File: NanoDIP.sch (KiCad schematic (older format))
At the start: 13 parts, among them SW1 SW_Push, U1 LM7805_TO220, U2 ATMEGA328P-PU, Y1 16 MHz

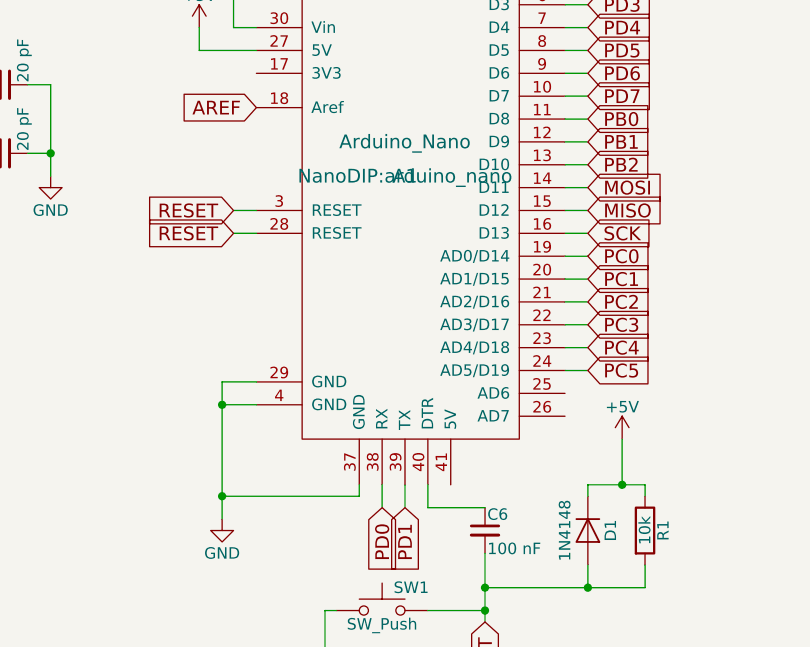
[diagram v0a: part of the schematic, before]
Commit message: Added 5V pin to program header
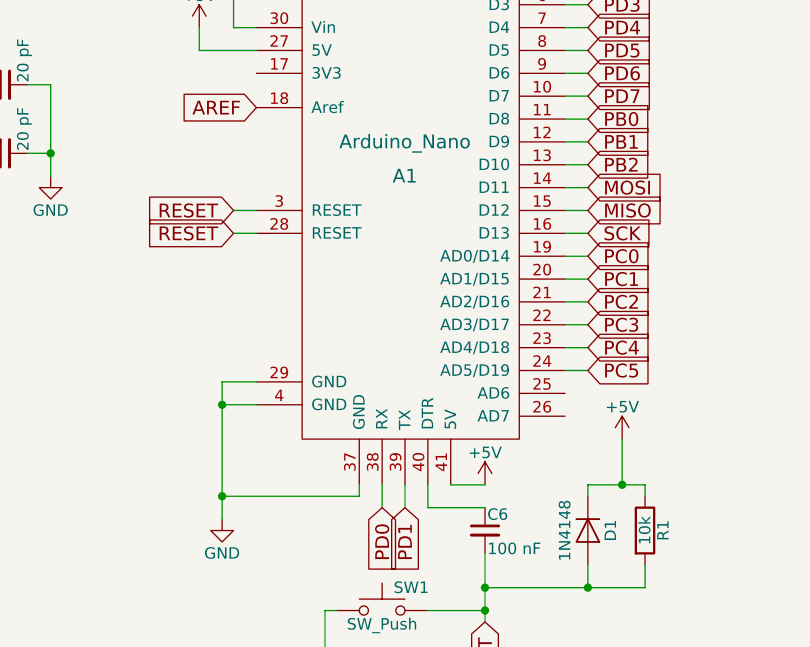
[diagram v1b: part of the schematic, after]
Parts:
- A1: footprint NanoDIP:arduino_nano -> (none)
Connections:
- net +5V: now also A1.41 (5V)
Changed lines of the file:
@@
 Text GLabel 4300 2950 2    60   Input ~ 0
 PC2
-$Comp
-L Arduino_Nano A1
-U 1 1 616CEBDE
-P 7000 2800
-F 0 "A1" H 7000 2800 60  0000 C CNN
-F 1 "Arduino_Nano" H 7000 2950 60  0000 C CNN
-F 2 "NanoDIP:arduino_nano" H 7000 2800 60  0000 C CNN
-F 3 "" H 7000 2800 60  0000 C CNN
-	1    7000 2800
-	1    0    0    -1
-$EndComp
 Text GLabel 4300 3350 2    60   Input ~ 0
 RESET
@@
 Text Notes 7800 6850 0    60   ~ 0
 Nano With ATMEGA328P-PU
+$Comp
+L Arduino_Nano A1
+U 1 1 616F122D
+P 7000 2800
+F 0 "A1" H 7000 2800 60  0000 C CNN
+F 1 "Arduino_Nano" H 7000 2950 60  0000 C CNN
+F 2 "" H 7000 2800 60  0000 C CNN
+F 3 "" H 7000 2800 60  0000 C CNN
+	1    7000 2800
+	1    0    0    -1
+$EndComp
+$Comp
+L +5V #PWR?
+U 1 1 616F12FD
+P 7350 4150
+F 0 "#PWR?" H 7350 4000 50  0001 C CNN
+F 1 "+5V" H 7350 4290 50  0000 C CNN
+F 2 "" H 7350 4150 50  0001 C CNN
+F 3 "" H 7350 4150 50  0001 C CNN
+	1    7350 4150
+	1    0    0    -1
+$EndComp
+Wire Wire Line
+	7350 4150 7200 4150
 $EndSCHEMATC

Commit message: JLCPCB order 2021-10-22
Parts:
- added C7: 100 nF, Capacitors_THT:C_Disc_D5.0mm_W2.5mm_P2.50mm, symbol C_Small
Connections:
- net +5V: now also C7.1
- net GND: now also C7.2
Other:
- moved on the sheet: C3
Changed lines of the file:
@@
 $EndComp
 $Comp
-L +5V #PWR01
+L +5V #PWR8
 U 1 1 616CD819
-P 2150 1850
-F 0 "#PWR01" H 2150 1700 50  0001 C CNN
-F 1 "+5V" H 2150 1990 50  0000 C CNN
-F 2 "" H 2150 1850 50  0001 C CNN
-F 3 "" H 2150 1850 50  0001 C CNN
-	1    2150 1850
+P 2300 1600
+F 0 "#PWR8" H 2300 1450 50  0001 C CNN
+F 1 "+5V" H 2300 1740 50  0000 C CNN
+F 2 "" H 2300 1600 50  0001 C CNN
+F 3 "" H 2300 1600 50  0001 C CNN
+	1    2300 1600
 	1    0    0    -1
 $EndComp
@@
 $EndComp
 $Comp
-L GND #PWR02
+L GND #PWR9
 U 1 1 616CE500
 P 5450 2800
-F 0 "#PWR02" H 5450 2550 50  0001 C CNN
+F 0 "#PWR9" H 5450 2550 50  0001 C CNN
 F 1 "GND" H 5450 2650 50  0000 C CNN
 F 2 "" H 5450 2800 50  0001 C CNN
@@
 $EndComp
 $Comp
-L GND #PWR03
+L GND #PWR7
 U 1 1 616CE54E
 P 2200 4350
-F 0 "#PWR03" H 2200 4100 50  0001 C CNN
+F 0 "#PWR7" H 2200 4100 50  0001 C CNN
 F 1 "GND" H 2200 4200 50  0000 C CNN
 F 2 "" H 2200 4350 50  0001 C CNN
@@
 $EndComp
 $Comp
-L GND #PWR04
+L GND #PWR3
 U 1 1 616CE64F
 P 1250 2300
-F 0 "#PWR04" H 1250 2050 50  0001 C CNN
+F 0 "#PWR3" H 1250 2050 50  0001 C CNN
 F 1 "GND" H 1250 2150 50  0000 C CNN
 F 2 "" H 1250 2300 50  0001 C CNN
@@
 $EndComp
 $Comp
-L +12V #PWR05
+L +12V #PWR1
 U 1 1 616CE6B5
 P 750 1700
-F 0 "#PWR05" H 750 1550 50  0001 C CNN
+F 0 "#PWR1" H 750 1550 50  0001 C CNN
 F 1 "+12V" H 750 1840 50  0000 C CNN
 F 2 "" H 750 1700 50  0001 C CNN
@@
 MISO
 $Comp
-L +5V #PWR06
+L +5V #PWR14
 U 1 1 616CEED4
 P 6750 950
-F 0 "#PWR06" H 6750 800 50  0001 C CNN
+F 0 "#PWR14" H 6750 800 50  0001 C CNN
 F 1 "+5V" H 6750 1090 50  0000 C CNN
 F 2 "" H 6750 950 50  0001 C CNN
@@
 SCK
 $Comp
-L +12V #PWR07
+L +12V #PWR12
 U 1 1 616CEF7A
 P 6250 1950
-F 0 "#PWR07" H 6250 1800 50  0001 C CNN
+F 0 "#PWR12" H 6250 1800 50  0001 C CNN
 F 1 "+12V" H 6250 2090 50  0000 C CNN
 F 2 "" H 6250 1950 50  0001 C CNN
@@
 L C_Small C3
 U 1 1 616CEFD3
-P 1850 2100
-F 0 "C3" H 1860 2170 50  0000 L CNN
-F 1 "100 nF" H 1860 2020 50  0000 L CNN
-F 2 "Capacitors_THT:C_Disc_D5.0mm_W2.5mm_P2.50mm" H 1850 2100 50  0001 C CNN
-F 3 "" H 1850 2100 50  0001 C CNN
-	1    1850 2100
-	1    0    0    -1
-$EndComp
-$Comp
-L GND #PWR08
+P 1800 2100
+F 0 "C3" H 1810 2170 50  0000 L CNN
+F 1 "100 nF" H 1810 2020 50  0000 L CNN
+F 2 "Capacitors_THT:C_Disc_D5.0mm_W2.5mm_P2.50mm" H 1800 2100 50  0001 C CNN
+F 3 "" H 1800 2100 50  0001 C CNN
+	1    1800 2100
+	1    0    0    -1
+$EndComp
+$Comp
+L GND #PWR5
 U 1 1 616CF07C
-P 1850 2300
-F 0 "#PWR08" H 1850 2050 50  0001 C CNN
-F 1 "GND" H 1850 2150 50  0000 C CNN
-F 2 "" H 1850 2300 50  0001 C CNN
-F 3 "" H 1850 2300 50  0001 C CNN
-	1    1850 2300
+P 1800 2300
+F 0 "#PWR5" H 1800 2050 50  0001 C CNN
+F 1 "GND" H 1800 2150 50  0000 C CNN
+F 2 "" H 1800 2300 50  0001 C CNN
+F 3 "" H 1800 2300 50  0001 C CNN
+	1    1800 2300
 	1    0    0    -1
 $EndComp
@@
 $EndComp
 $Comp
-L GND #PWR09
+L GND #PWR2
 U 1 1 616CF17C
 P 750 2300
-F 0 "#PWR09" H 750 2050 50  0001 C CNN
+F 0 "#PWR2" H 750 2050 50  0001 C CNN
 F 1 "GND" H 750 2150 50  0000 C CNN
 F 2 "" H 750 2300 50  0001 C CNN
@@
 $EndComp
 $Comp
-L GND #PWR010
+L GND #PWR4
 U 1 1 616CF301
 P 1600 2300
-F 0 "#PWR010" H 1600 2050 50  0001 C CNN
+F 0 "#PWR4" H 1600 2050 50  0001 C CNN
 F 1 "GND" H 1600 2150 50  0000 C CNN
 F 2 "" H 1600 2300 50  0001 C CNN
@@
 $EndComp
 $Comp
-L GND #PWR011
+L GND #PWR11
 U 1 1 616CF3B4
 P 6200 4300
-F 0 "#PWR011" H 6200 4050 50  0001 C CNN
+F 0 "#PWR11" H 6200 4050 50  0001 C CNN
 F 1 "GND" H 6200 4150 50  0000 C CNN
 F 2 "" H 6200 4300 50  0001 C CNN
@@
 $EndComp
 $Comp
-L +5V #PWR012
+L +5V #PWR17
 U 1 1 616CFBD7
 P 7950 3950
-F 0 "#PWR012" H 7950 3800 50  0001 C CNN
+F 0 "#PWR17" H 7950 3800 50  0001 C CNN
 F 1 "+5V" H 7950 4090 50  0000 C CNN
 F 2 "" H 7950 3950 50  0001 C CNN
@@
 $EndComp
 $Comp
-L GND #PWR013
+L GND #PWR16
 U 1 1 616CFC75
 P 7400 1350
-F 0 "#PWR013" H 7400 1100 50  0001 C CNN
+F 0 "#PWR16" H 7400 1100 50  0001 C CNN
 F 1 "GND" H 7400 1200 50  0000 C CNN
 F 2 "" H 7400 1350 50  0001 C CNN
@@
 	1550 1900 2300 1900
 Wire Wire Line
-	2150 1850 2150 2200
-Wire Wire Line
-	2150 2200 2300 2200
-Connection ~ 2150 1900
-Wire Wire Line
 	4300 1900 4200 1900
 Wire Wire Line
@@
 	6250 2150 6350 2150
 Wire Wire Line
-	1850 2300 1850 2200
-Wire Wire Line
-	1850 2000 1850 1900
-Connection ~ 1850 1900
+	1800 2300 1800 2200
 Connection ~ 750  1900
 Wire Wire Line
@@
 	7100 4250 7100 4150
 Wire Wire Line
-	7350 4750 7350 4450
+	7350 4450 7350 4750
 Wire Wire Line
 	7800 4500 7800 4600
@@
 Connection ~ 7800 4600
 Wire Wire Line
-	8050 4200 8050 4150
-Wire Wire Line
-	8050 4150 7800 4150
+	8050 4150 8050 4200
+Wire Wire Line
+	7800 4150 8050 4150
 Wire Wire Line
 	7800 4150 7800 4200
@@
 Connection ~ 7350 4700
 $Comp
-L GND #PWR014
+L GND #PWR13
 U 1 1 616D110E
 P 6650 4950
-F 0 "#PWR014" H 6650 4700 50  0001 C CNN
+F 0 "#PWR13" H 6650 4700 50  0001 C CNN
 F 1 "GND" H 6650 4800 50  0000 C CNN
 F 2 "" H 6650 4950 50  0001 C CNN
@@
 AREF
 $Comp
-L +5V #PWR015
+L +5V #PWR10
 U 1 1 616D1771
 P 6100 2150
-F 0 "#PWR015" H 6100 2000 50  0001 C CNN
+F 0 "#PWR10" H 6100 2000 50  0001 C CNN
 F 1 "+5V" H 6100 2290 50  0000 C CNN
 F 2 "" H 6100 2150 50  0001 C CNN
@@
 $EndComp
 $Comp
-L +5V #PWR?
+L +5V #PWR15
 U 1 1 616F12FD
 P 7350 4150
-F 0 "#PWR?" H 7350 4000 50  0001 C CNN
+F 0 "#PWR15" H 7350 4000 50  0001 C CNN
 F 1 "+5V" H 7350 4290 50  0000 C CNN
 F 2 "" H 7350 4150 50  0001 C CNN
@@
 Wire Wire Line
 	7350 4150 7200 4150
+Wire Wire Line
+	2300 1600 2300 2200
+Wire Wire Line
+	2350 1600 2300 1600
+Connection ~ 2300 1900
+Wire Wire Line
+	1800 2000 1800 1900
+Connection ~ 1800 1900
+$Comp
+L C_Small C7
+U 1 1 61724C51
+P 2100 2100
+F 0 "C7" H 2110 2170 50  0000 L CNN
+F 1 "100 nF" H 2110 2020 50  0000 L CNN
+F 2 "Capacitors_THT:C_Disc_D5.0mm_W2.5mm_P2.50mm" H 2100 2100 50  0001 C CNN
+F 3 "" H 2100 2100 50  0001 C CNN
+	1    2100 2100
+	1    0    0    -1
+$EndComp
+$Comp
+L GND #PWR6
+U 1 1 61724CC4
+P 2100 2250
+F 0 "#PWR6" H 2100 2000 50  0001 C CNN
+F 1 "GND" H 2100 2100 50  0000 C CNN
+F 2 "" H 2100 2250 50  0001 C CNN
+F 3 "" H 2100 2250 50  0001 C CNN
+	1    2100 2250
+	1    0    0    -1
+$EndComp
+Wire Wire Line
+	2100 2250 2100 2200
+Wire Wire Line
+	2100 2000 2100 1900
+Connection ~ 2100 1900
 $EndSCHEMATC
